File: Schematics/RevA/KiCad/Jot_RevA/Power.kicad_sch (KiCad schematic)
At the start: 4 parts, among them J1 USB-C, J2 Battery

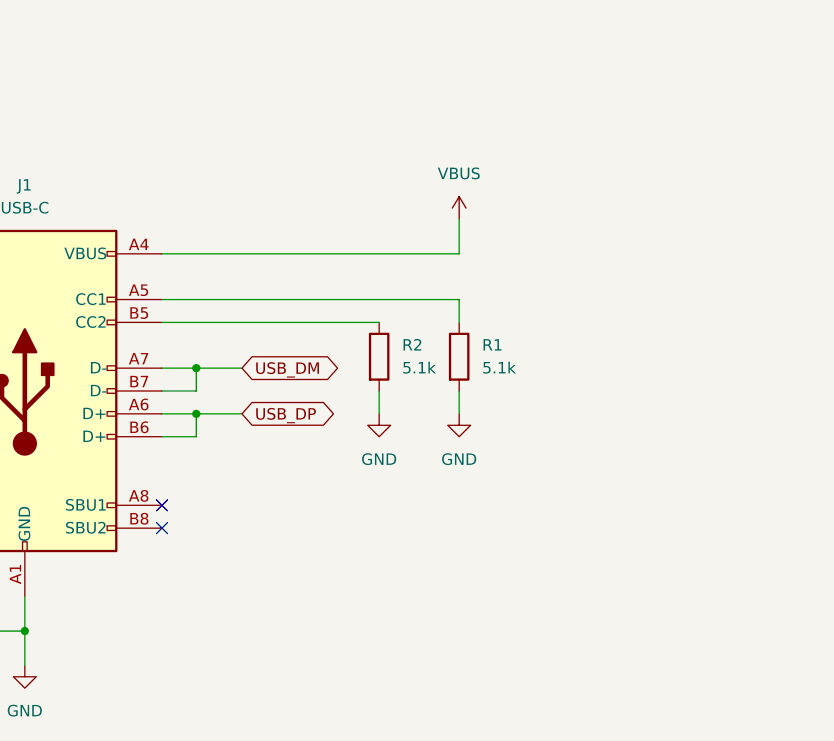
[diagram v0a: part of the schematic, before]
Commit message: KiCad Power: wire U10 USBLC6 ESD between USB-C data pins and labels
Co-Authored-By: Claude Opus 5.5 <noreply@anthropic.com>
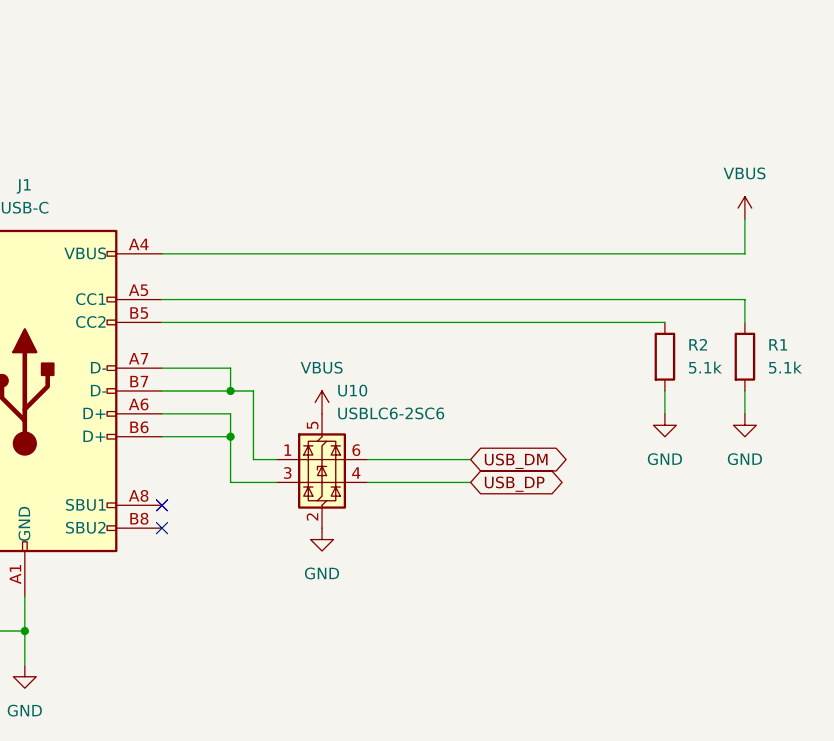
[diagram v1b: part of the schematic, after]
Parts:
- added U10: USBLC6-2SC6, Package_TO_SOT_SMD:SOT-23-6, symbol Power_Protection:USBLC6-2SC6
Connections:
- net GND: now also U10.2 (GND)
- net USB_DM: now also U10.6 (I/O1); no longer J1.A7 (D-), J1.B7 (D-)
- net USB_DP: now also U10.4 (I/O2); no longer J1.A6 (D+), J1.B6 (D+)
- net VBUS: now also U10.5 (VBUS)
- new net: J1.A7 (D-), J1.B7 (D-), U10.1 (I/O1)
- new net: J1.A6 (D+), J1.B6 (D+), U10.3 (I/O2)
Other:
- moved on the sheet: R1, R2

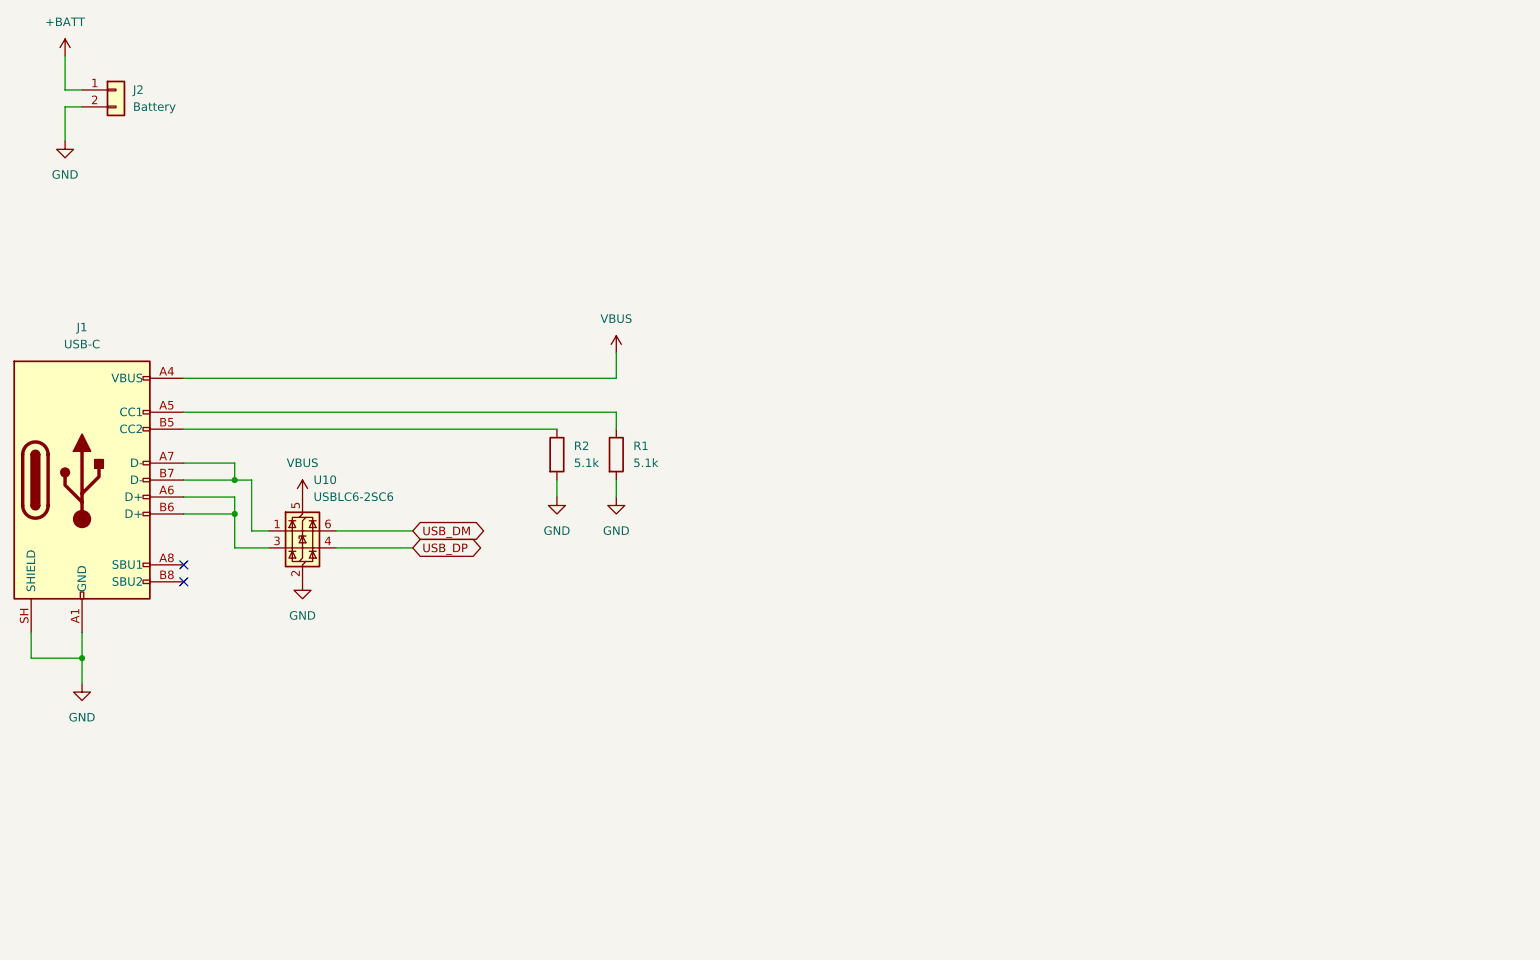
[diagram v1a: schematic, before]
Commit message: KiCad Power: charger, battery, 3.3 V LDO and fuel gauge
- Project symbol library Jot.kicad_sym with BQ25101, TPS7A0233 and
  MAX17048, pinouts taken from their datasheets
- Power sheet: BQ25101 charger (680R ISET ~200 mA, 10k TS), charge LED,
  battery connector, TPS7A0233 3.3 V LDO (EN tied to IN), MAX17048 fuel
  gauge on I2C with FG_ALRT, input/output caps, PWR_FLAGs on VBUS/GND
- Pin list net names now match KiCad power symbols (+BATT, +3V3, VBUS)

Co-Authored-By: Claude Opus 5.5 <noreply@anthropic.com>
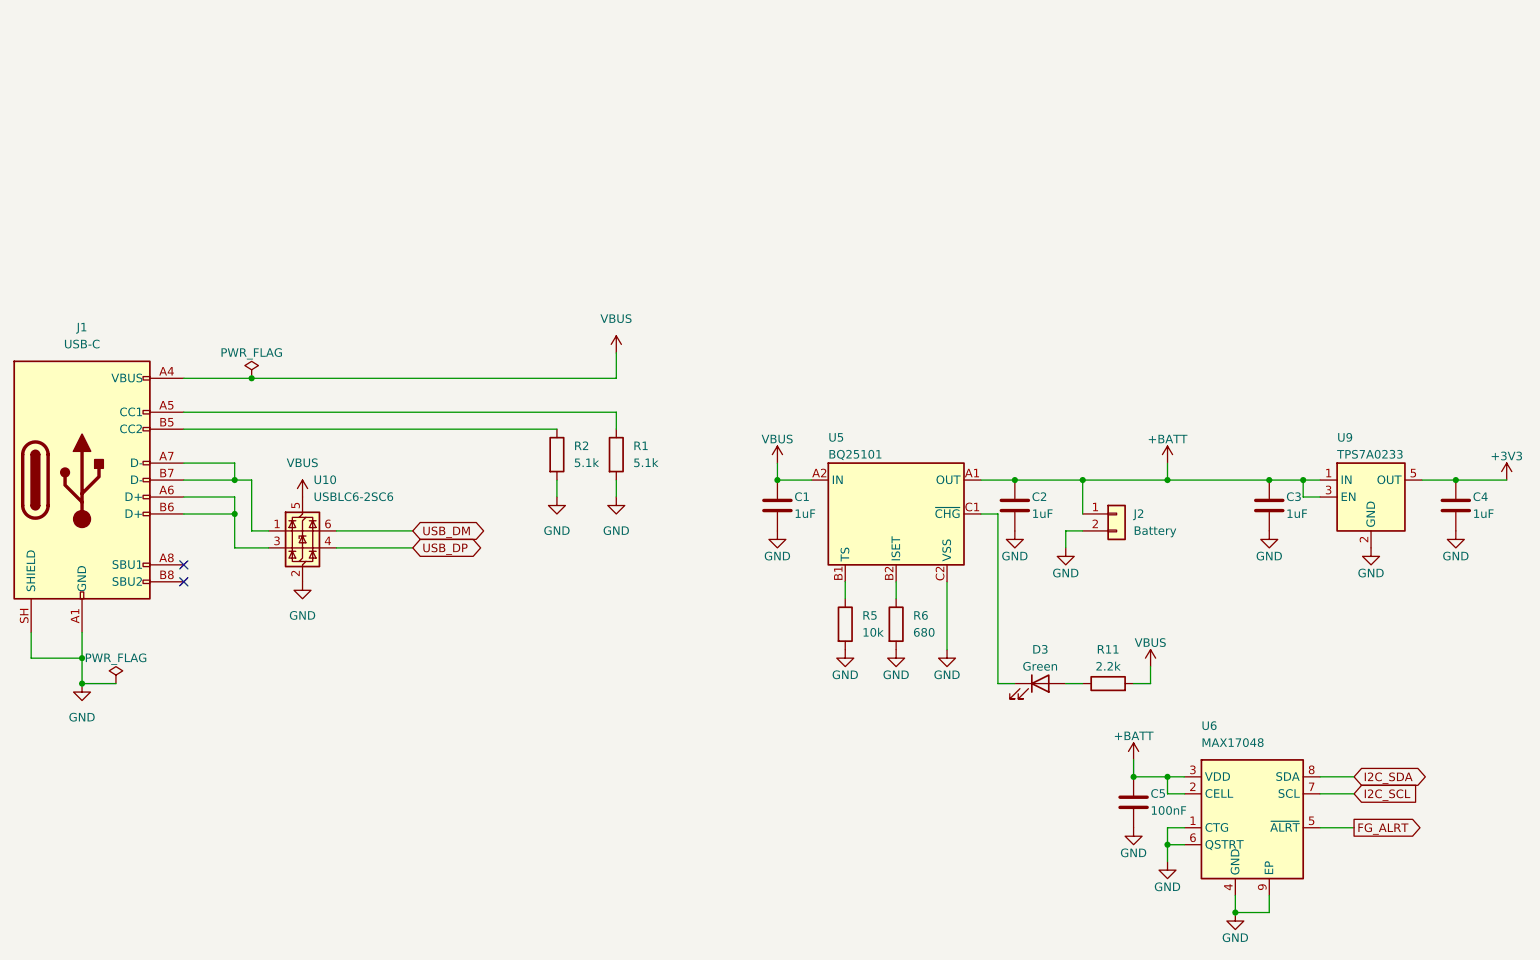
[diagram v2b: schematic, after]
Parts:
- added C1, C2, C3, C4: 1uF, Capacitor_SMD:C_0402_1005Metric, symbol Device:C
- added C5: 100nF, Capacitor_SMD:C_0402_1005Metric, symbol Device:C
- added D3: Green, LED_SMD:LED_0603_1608Metric, symbol Device:LED
- added R11: 2.2k, Resistor_SMD:R_0402_1005Metric, symbol Device:R
- added R5: 10k, Resistor_SMD:R_0402_1005Metric, symbol Device:R
- added R6: 680, Resistor_SMD:R_0402_1005Metric, symbol Device:R
- added U5: BQ25101, symbol Jot:BQ25101
- added U6: MAX17048, symbol Jot:MAX17048
- added U9: TPS7A0233, Package_TO_SOT_SMD:SOT-23-5, symbol Jot:TPS7A0233
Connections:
- net +BATT: now also C2.1, C3.1, C5.1, U5.A1 (OUT), U6.2 (CELL), U6.3 (VDD), U9.1 (IN), U9.3 (EN)
- net GND: now also C1.2, C2.2, C3.2, C4.2, C5.2, R5.2, R6.2, U5.C2 (VSS), U6.1 (CTG), U6.4 (GND), U6.6 (QSTRT), U6.9 (EP), U9.2 (GND)
- net VBUS: now also C1.1, R11.2, U5.A2 (IN)
- new net: R6.1, U5.B2 (ISET)
- new net: R5.1, U5.B1 (TS)
- new net: D3.2 (A), R11.1
- new net: D3.1 (K), U5.C1 (~{CHG})
- new net +3V3: C4.1, U9.5 (OUT)
- new net FG_ALRT: U6.5 (~{ALRT})
- new net I2C_SCL: U6.7 (SCL)
- new net I2C_SDA: U6.8 (SDA)
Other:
- moved on the sheet: J2

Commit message: KiCad: tidy MCU power cluster and spacing; fill MCU/Power title blocks
Co-Authored-By: Claude Opus 5.5 <noreply@anthropic.com>
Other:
- company: JC -> James Donal Cronin
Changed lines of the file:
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@@
 		(date "2026-10-02")
 		(rev "A")
-		(company "JC")
+		(company "James Donal Cronin")
+		(comment 1 "JOT-HW-001: handheld push-to-talk voice capture")
 	)
 	(junction

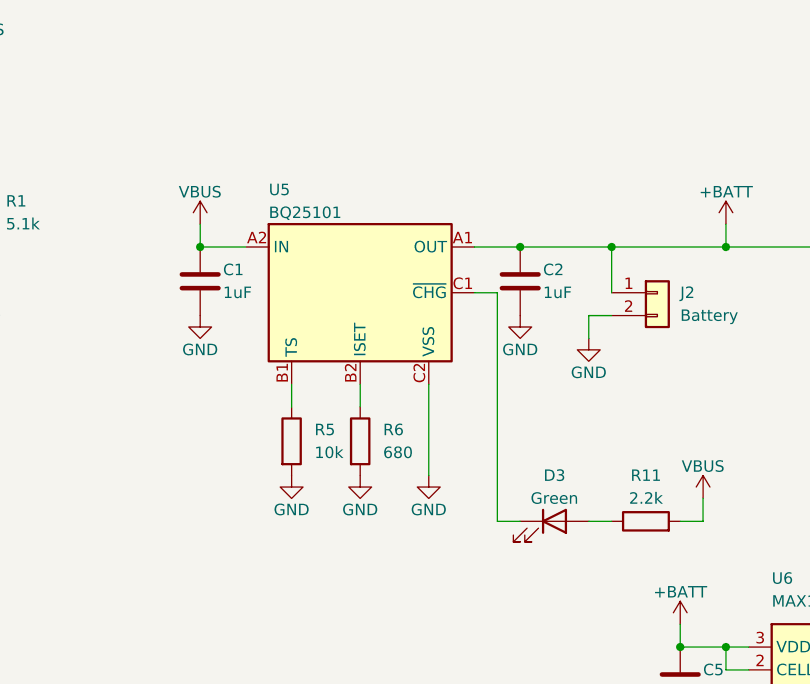
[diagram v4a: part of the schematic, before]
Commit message: Charger: BQ25101 (0.4 mm BGA, not JLCPCB Economic assemblable) -> MCP73831 SOT-23-5; R6 5.1k PROG (196 mA), R5 removed, C1/C2 4.7 uF; BOM, pin list, architecture draft 4
Co-Authored-By: Claude Opus 5.5 <noreply@anthropic.com>
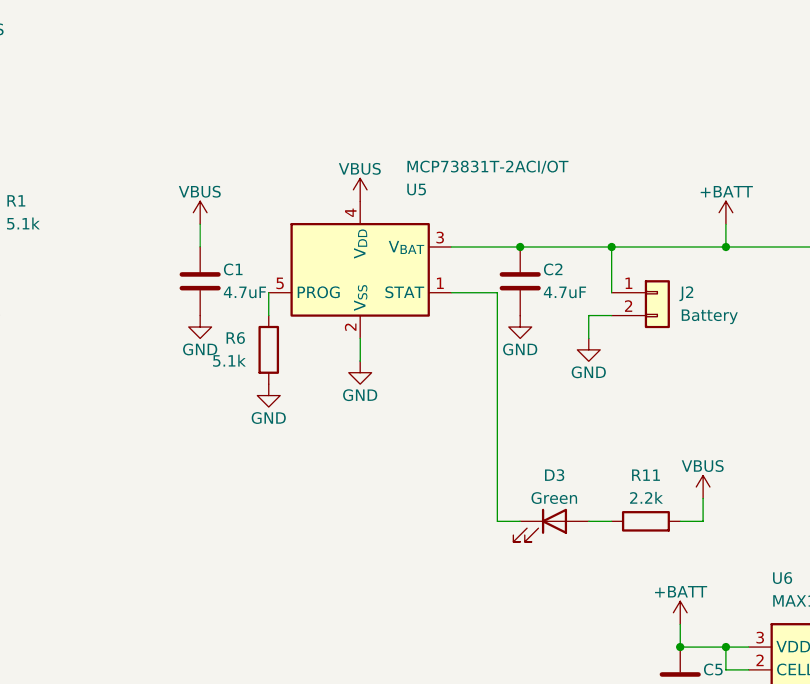
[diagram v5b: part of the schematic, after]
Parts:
- removed R5: 10k, Resistor_SMD:R_0402_1005Metric, symbol Device:R
- removed U5: BQ25101, symbol Jot:BQ25101
- added U5: MCP73831T-2ACI/OT, Package_TO_SOT_SMD:SOT-23-5, symbol Battery_Management:MCP73831-2-OT
- C1, C2: value 1uF -> 4.7uF
- R6: value 680 -> 5.1k; footprint Resistor_SMD:R_0402_1005Metric -> (none)
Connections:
- net +BATT: now also U5.3 (V_{BAT})
- net GND: now also U5.2 (V_{SS})
- net VBUS: now also U5.4 (V_{DD})
- net at R6.1: now also U5.5 (PROG)
- net at D3.1 (K): now also U5.1 (STAT)
